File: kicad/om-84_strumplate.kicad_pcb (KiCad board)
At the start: 2 copper layers, 117.2 x 151.8 mm, 0 parts

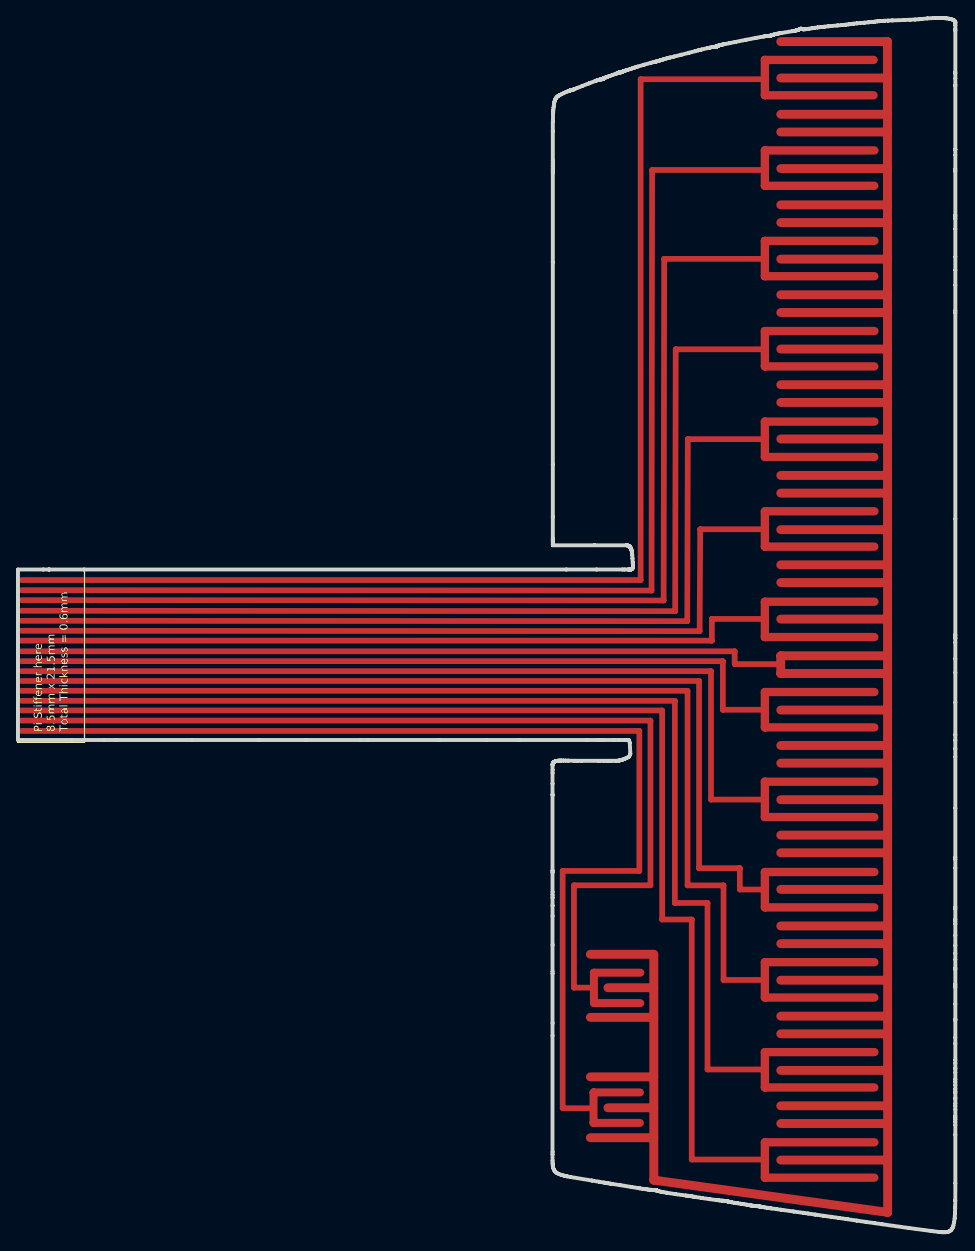
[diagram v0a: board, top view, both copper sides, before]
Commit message: Fixed coverlay after JLCPCB feedback
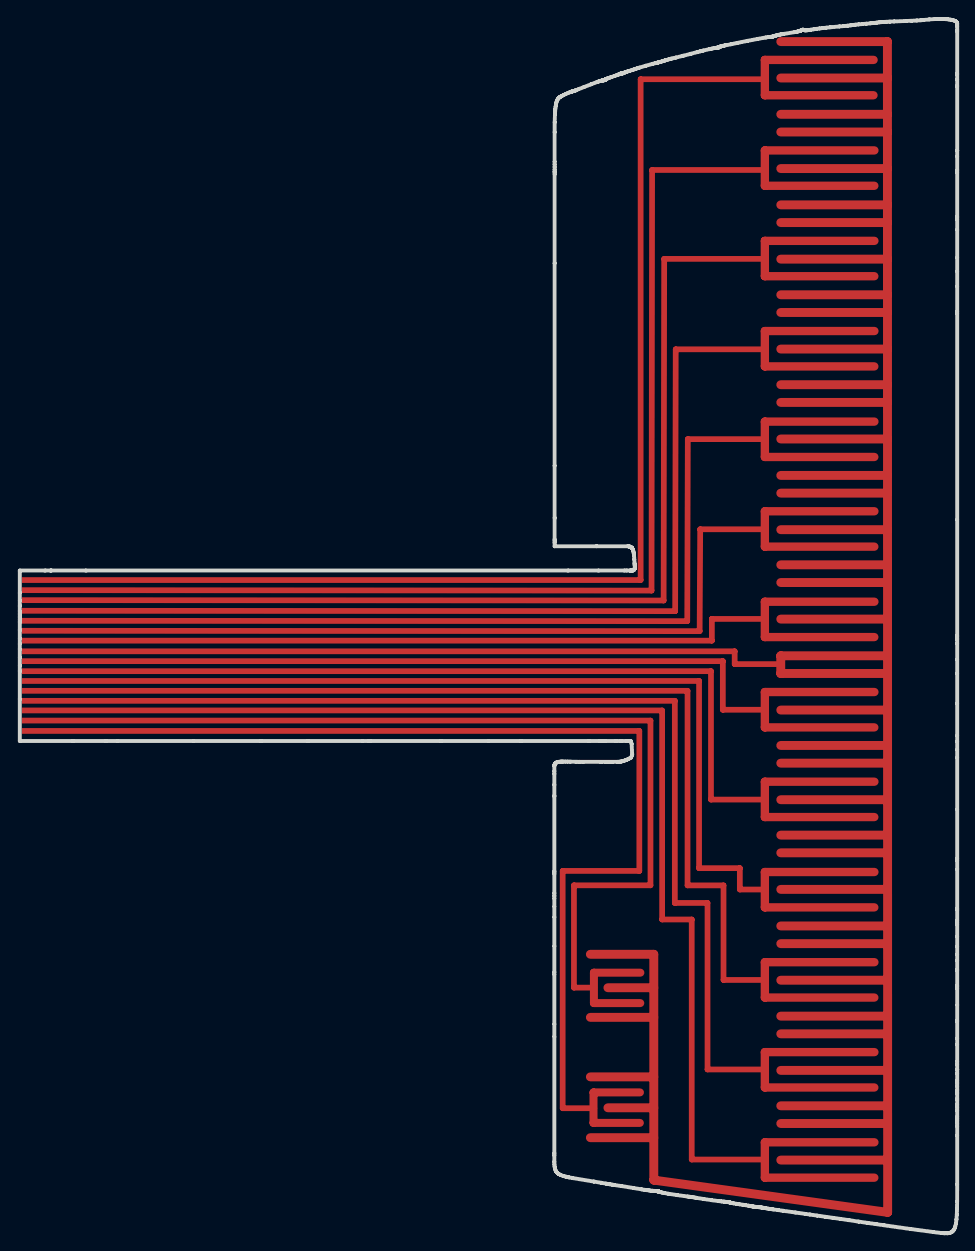
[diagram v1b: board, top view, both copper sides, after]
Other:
- board text added: "Add Stiffener Here 8.5mm x 21.5mm Stiffener: Polyimide Total Thickness: 0.6mm"
- board text removed: "Pi Stiffener here 8.5mm x 21.5mm Total Thickness = 0.6mm"

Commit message: Updated Gerbers, V1.0 confirmed working!
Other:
- board text added: "Add Stiffener Here 8.5mm x 21.5mm Stiffener: Polyimide Total Thickness (Gold Finger): 0.3mm"
- board text removed: "Add Stiffener Here 8.5mm x 21.5mm Stiffener: Polyimide Total Thickness: 0.6mm"
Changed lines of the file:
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@@
 		(layer "User.1")
 	)
-	(gr_text "Add Stiffener Here\n8.5mm x 21.5mm\nStiffener: Polyimide\nTotal Thickness: 0.6mm"
+	(gr_text "Add Stiffener Here\n8.5mm x 21.5mm\nStiffener: Polyimide\nTotal Thickness (Gold Finger): 0.3mm"
 		(at 78.6 166.84 0)
 		(layer "User.1")
